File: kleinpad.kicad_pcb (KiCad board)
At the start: 2 copper layers, 79 x 79 mm, 31 parts, among them J1 Conn_01x02, J2 Conn_01x05, SW1 SW_Push, SW2 RotaryEncoder_Switch, U1 SuperMini nRF52840

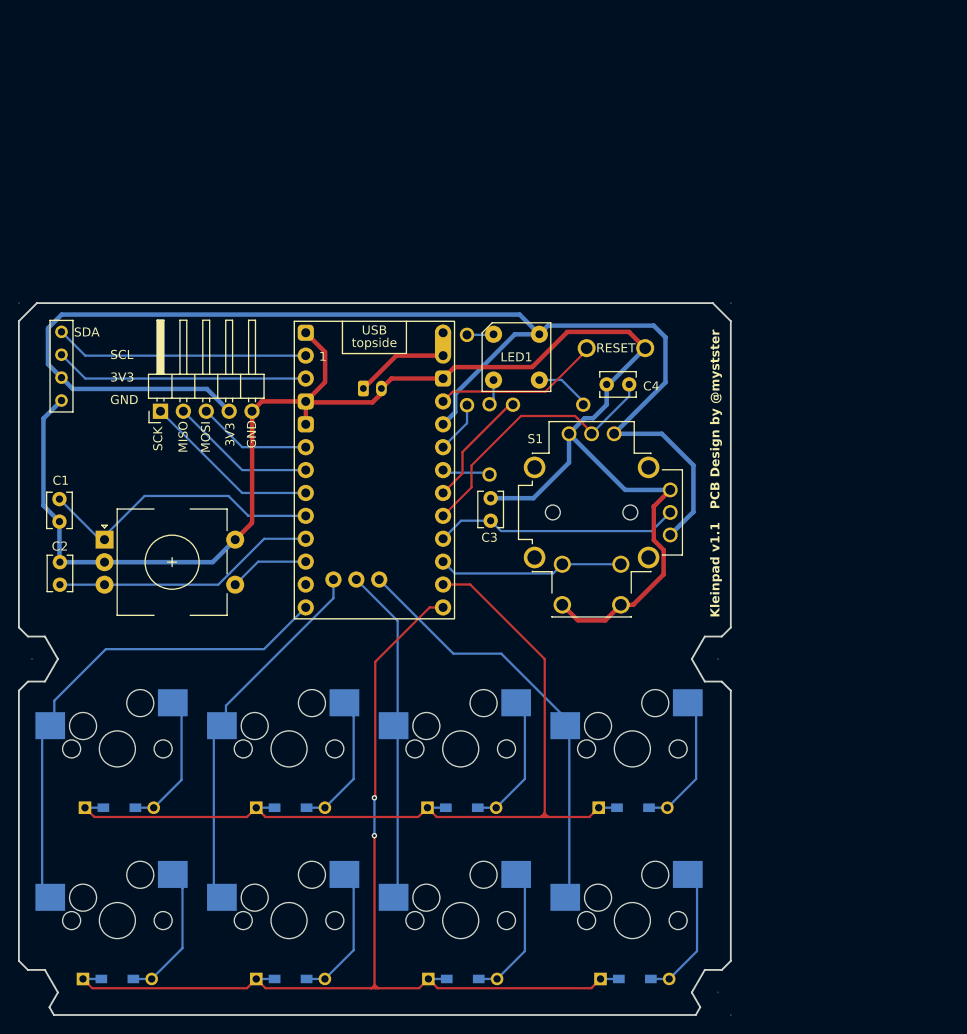
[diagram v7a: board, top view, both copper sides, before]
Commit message: fix: ダイオードのスルーホールがキースイッチに干渉する Fixes #3
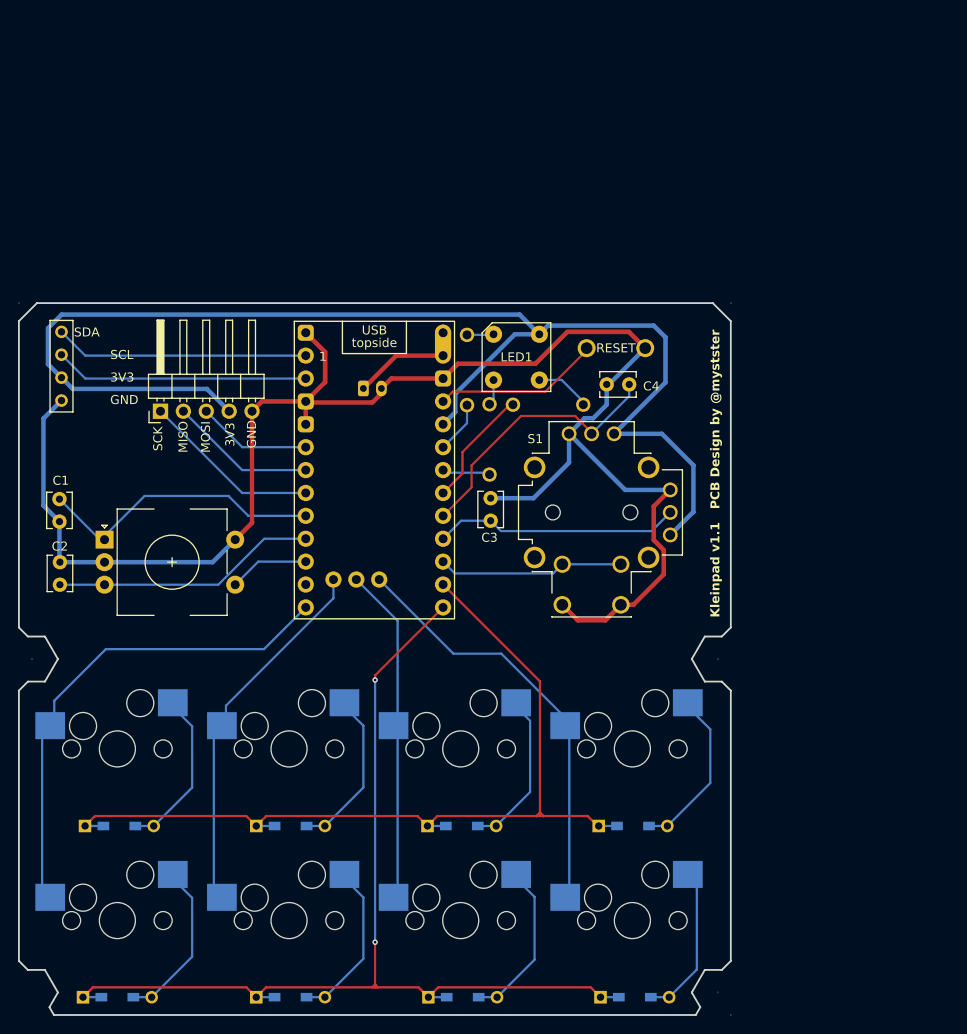
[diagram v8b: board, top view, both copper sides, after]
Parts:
- moved D1 2.02 mm to (112.4, 118.5)
- moved D3 2.02 mm to (131.4, 118.5)
- moved D5 2.02 mm to (150.4, 118.5)
- moved D7 2.02 mm to (169.4, 118.5)
- moved D2 2.02 mm to (112.2, 137.5)
- moved D4 2.02 mm to (131.4, 137.5)
- moved D6 2.02 mm to (150.5, 137.5)
- moved D8 2.02 mm to (169.6, 137.5)
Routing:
- net Net-(D7-A): track 15.6 -> 18.9 mm
- net Net-(D1-A): track 15.6 -> 18.6 mm
- net Net-(D3-A): track 15.6 -> 18.5 mm
- net Net-(D4-A): track 15.6 -> 18.5 mm
- net Net-(D2-A): track 15.7 -> 18.6 mm
- net Net-(D6-A): track 15.5 -> 18.4 mm
- net Net-(D5-A): track 15.6 -> 18.1 mm
- net ROW_1: track 101.3 -> 99.2 mm
- net Net-(D8-A): track 15.5 -> 17.5 mm
- net ROW_2: track 115.5 -> 114.4 mm
- net GND: track 181.1 -> 180.1 mm
- net RE_A: track 32.4 -> 31.5 mm
- net Net-(LED1-BK): track 6.22 -> 5.64 mm
